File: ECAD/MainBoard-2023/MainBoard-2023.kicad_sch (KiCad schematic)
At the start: 69 parts, among them J1 XT60, J10 Conn_01x14, J11 Conn_01x03, J12 Conn_01x04, J13 Conn_01x03, J14 Conn_01x03, J15 Conn_01x03, J2 Conn_01x04, J20 BAU, J21 BAU, J22 Conn_01x04, J23 Conn_01x02, J24 Conn_01x07, J26 BAU, J27 BAU, J28 Conn_01x02, J29 Conn_01x02, J3 ConStep1, J30 Conn_01x03, J32 Conn_01x02, J37 Conn_01x02, J38 Conn_01x02, J39 Conn_01x02, J4 Conn_01x02, J40 Conn_01x02, J5 ConStep1, J6 ConStep1, J7 XT30, J8 Conn_01x02, J9 XT60, K1 CB1-P-24V, U1 Teensy3.5_All_Pins, U2 R-78B3.3-2.0, U4 R-78B5.0-2.0

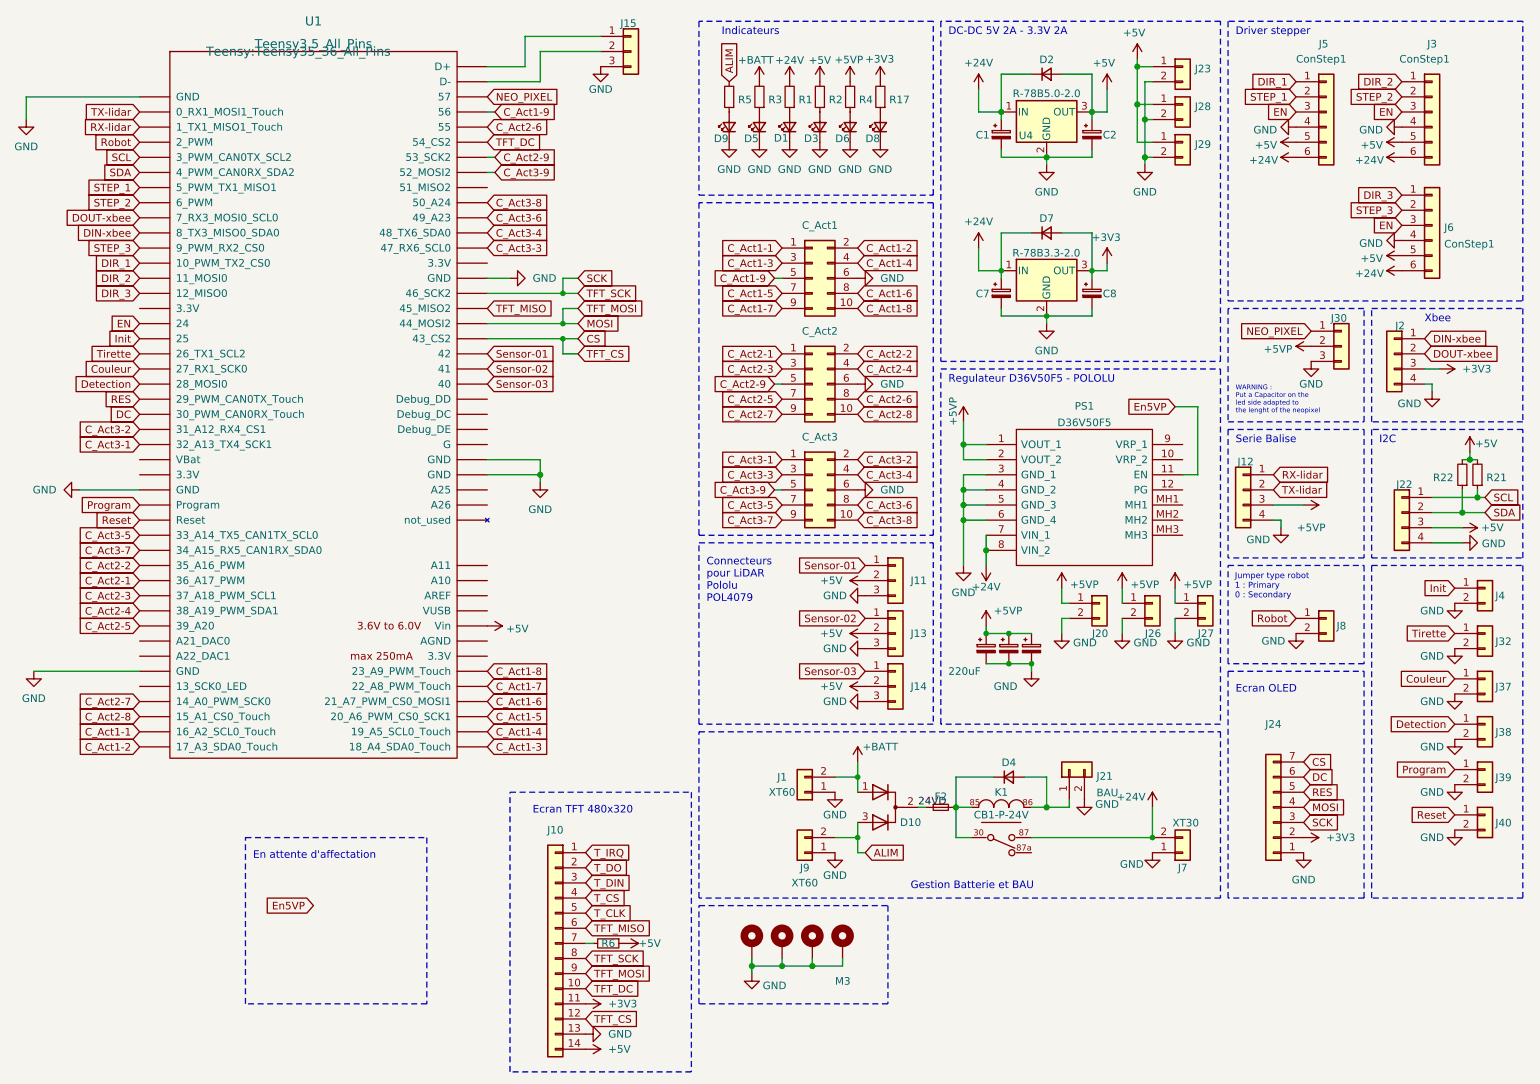
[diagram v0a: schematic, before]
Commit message: add connectors - modify pinout
add 3 power connectors XT-30 24V
modify pinout to have a minimum of 2 pwm for each sattellite connectors
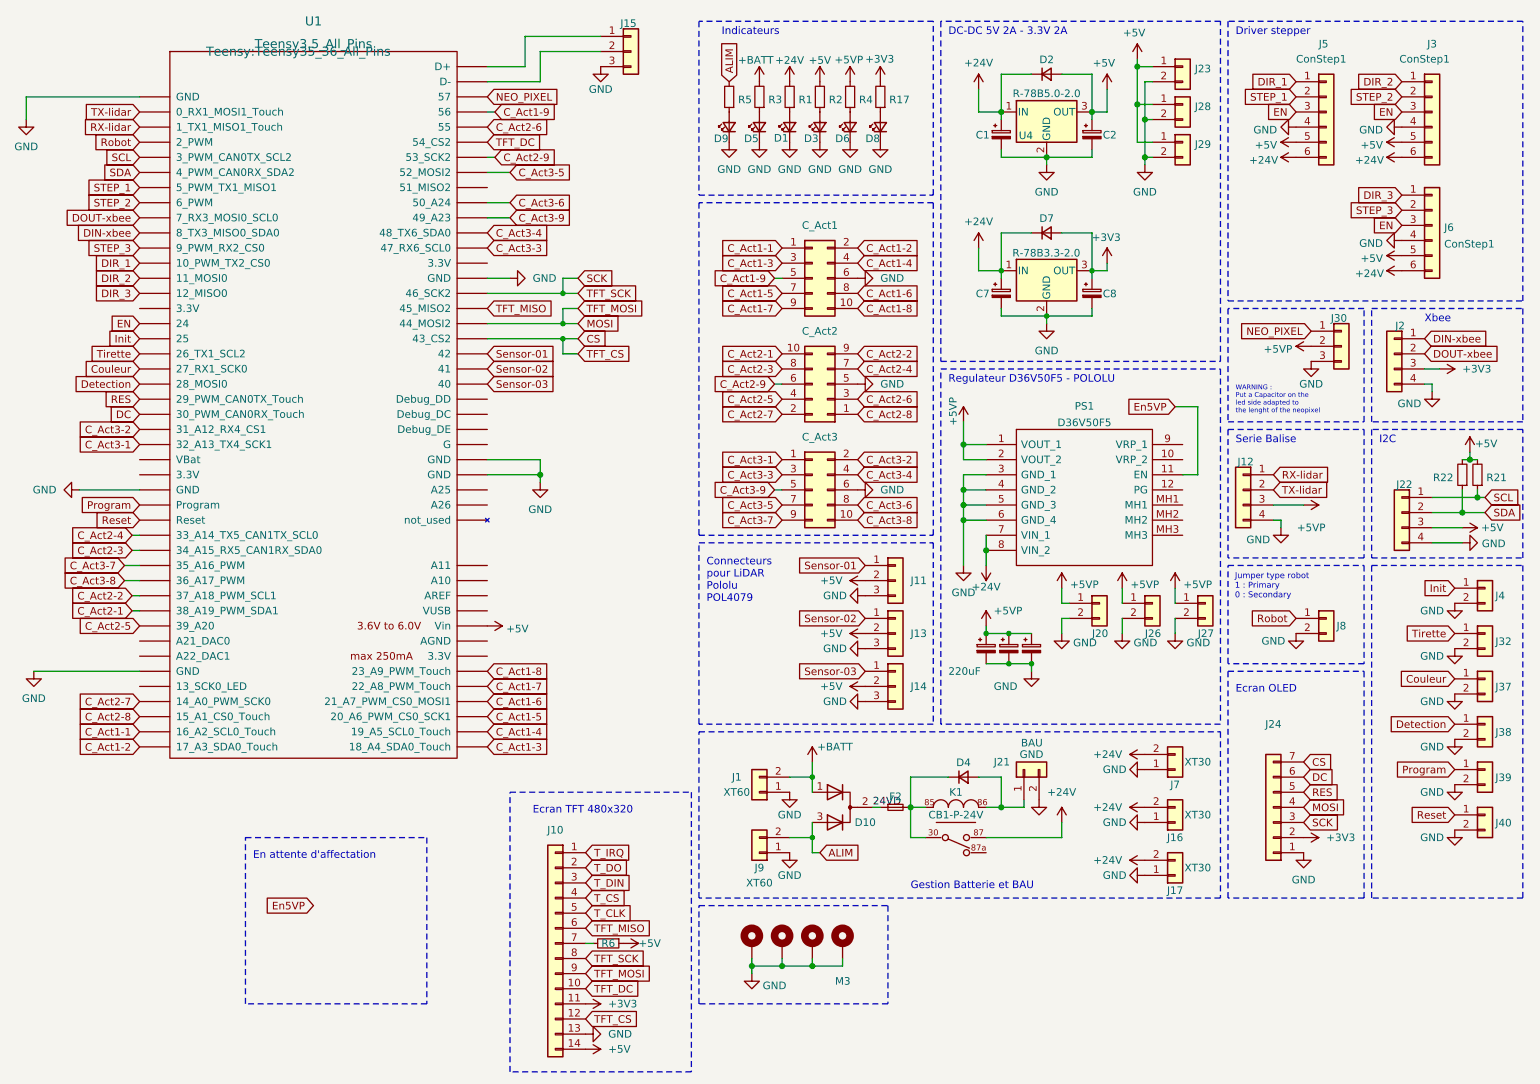
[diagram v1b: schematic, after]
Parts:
- added J16, J17: XT30, Connector_AMASS:AMASS_XT30UPB-F_1x02_P5.0mm_Vertical, symbol Connector_Generic:Conn_01x02
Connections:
- net +24V: now also J16.2 (Pin_2), J17.2 (Pin_2)
- net C_Act2-1: now also C_Act2.10 (Pin_10), U1.35 (38_A19_PWM_SDA1); no longer C_Act2.1 (Pin_1), U1.33 (36_A17_PWM)
- net C_Act2-2: now also C_Act2.9 (Pin_9), U1.34 (37_A18_PWM_SCL1); no longer C_Act2.2 (Pin_2), U1.32 (35_A16_PWM)
- net C_Act2-3: now also C_Act2.8 (Pin_8), U1.31 (34_A15_RX5_CAN1RX_SDA0); no longer C_Act2.3 (Pin_3), U1.34 (37_A18_PWM_SCL1)
- net C_Act2-4: now also C_Act2.7 (Pin_7), U1.30 (33_A14_TX5_CAN1TX_SCL0); no longer C_Act2.4 (Pin_4), U1.35 (38_A19_PWM_SDA1)
- net C_Act2-5: now also C_Act2.4 (Pin_4); no longer C_Act2.7 (Pin_7)
- net C_Act2-6: now also C_Act2.3 (Pin_3); no longer C_Act2.8 (Pin_8)
- net C_Act2-7: now also C_Act2.2 (Pin_2); no longer C_Act2.9 (Pin_9)
- net C_Act2-8: now also C_Act2.1 (Pin_1); no longer C_Act2.10 (Pin_10)
- net C_Act2-9: now also C_Act2.6 (Pin_6); no longer C_Act2.5 (Pin_5)
- net C_Act3-5: now also U1.81 (52_MOSI2); no longer U1.30 (33_A14_TX5_CAN1TX_SCL0)
- net C_Act3-6: now also U1.79 (50_A24); no longer U1.78 (49_A23)
- net C_Act3-7: now also U1.32 (35_A16_PWM); no longer U1.31 (34_A15_RX5_CAN1RX_SDA0)
- net C_Act3-8: now also U1.33 (36_A17_PWM); no longer U1.79 (50_A24)
- net C_Act3-9: now also U1.78 (49_A23); no longer U1.81 (52_MOSI2)
- net GND: now also C_Act2.5 (Pin_5), J16.1 (Pin_1), J17.1 (Pin_1); no longer C_Act2.6 (Pin_6)
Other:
- moved on the sheet: C_Act2, D10, D4, F2, J1, J21, J9, K1

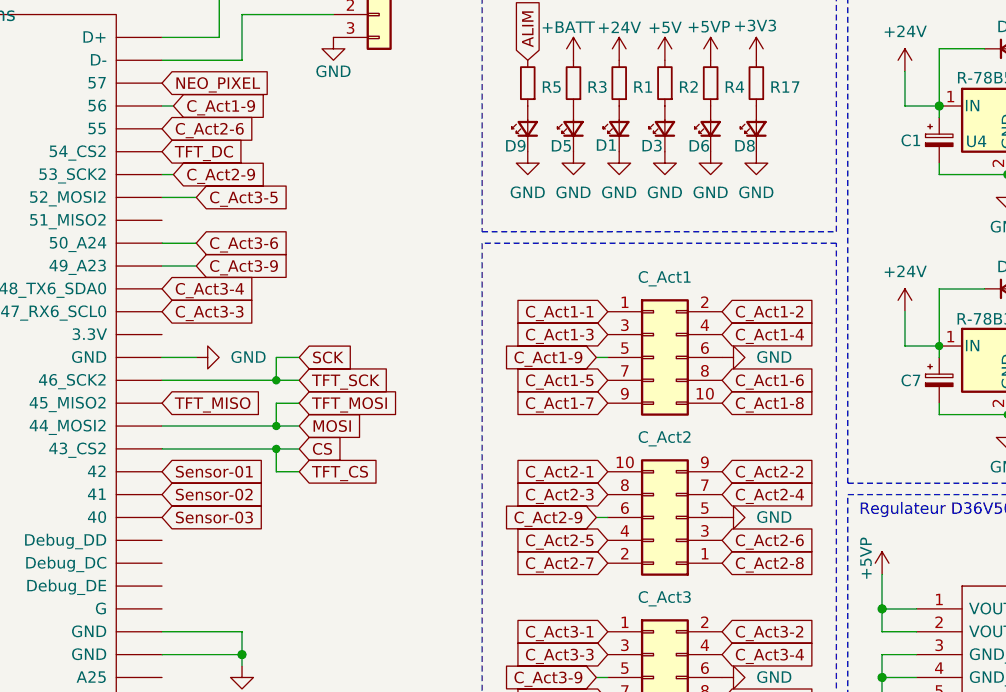
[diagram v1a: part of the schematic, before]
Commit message: Change Pinout
Change pinout for the Satellite connectors
- 2 PWM
- 4 analog
- 3 other (mix digital/analog/pwm depending on the connector)
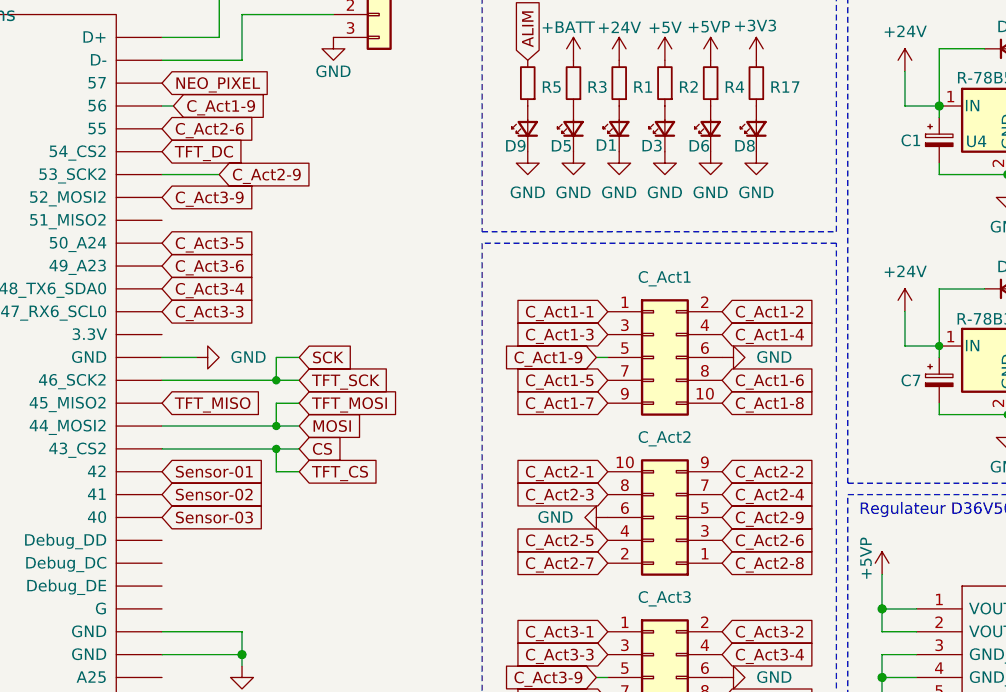
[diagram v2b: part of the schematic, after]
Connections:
- net C_Act2-9: now also C_Act2.5 (Pin_5); no longer C_Act2.6 (Pin_6)
- net C_Act3-5: now also U1.79 (50_A24); no longer U1.81 (52_MOSI2)
- net C_Act3-6: now also U1.78 (49_A23); no longer U1.79 (50_A24)
- net C_Act3-9: now also U1.81 (52_MOSI2); no longer U1.78 (49_A23)
- net GND: now also C_Act2.6 (Pin_6); no longer C_Act2.5 (Pin_5)
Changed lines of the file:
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@@
     (stroke (width 0) (type default) (color 0 0 0 0))
   )
-  (wire (pts (xy 109.22 40.64) (xy 107.95 40.64))
+  (wire (pts (xy 114.3 40.64) (xy 107.95 40.64))
     (stroke (width 0) (type default) (color 0 0 0 0))
   )
@@
     (stroke (width 0) (type dash) (color 0 0 0 0))
   )
-  (wire (pts (xy 111.76 43.18) (xy 107.95 43.18))
-    (stroke (width 0) (type default) (color 0 0 0 0))
-  )
   (polyline (pts (xy 232.41 165.1) (xy 232.41 127))
     (stroke (width 0) (type dash) (color 0 0 0 0))
@@
     (stroke (width 0) (type dash) (color 0 0 0 0))
   )
-  (wire (pts (xy 111.76 50.8) (xy 107.95 50.8))
-    (stroke (width 0) (type default) (color 0 0 0 0))
-  )
   (polyline (pts (xy 182.88 48.26) (xy 143.51 48.26))
     (stroke (width 0) (type dash) (color 0 0 0 0))
@@
     (stroke (width 0) (type default) (color 0 0 0 0))
   )
-  (wire (pts (xy 111.76 48.26) (xy 107.95 48.26))
-    (stroke (width 0) (type default) (color 0 0 0 0))
-  )
   (wire (pts (xy 48.26 114.3) (xy 49.53 114.3))
     (stroke (width 0) (type default) (color 0 0 0 0))
@@
     (stroke (width 0) (type solid) (color 0 0 0 0))
   )
-  (wire (pts (xy 156.21 78.74) (xy 157.48 78.74))
-    (stroke (width 0) (type default) (color 0 0 0 0))
-  )
   (wire (pts (xy 218.44 27.94) (xy 218.44 34.29))
     (stroke (width 0) (type solid) (color 0 0 0 0))
@@
     )
   )
-  (global_label "C_Act2-9" (shape input) (at 156.21 78.74 180) (fields_autoplaced)
-    (effects (font (size 1.27 1.27)) (justify right))
-    (property "Intersheet References" "${INTERSHEET_REFS}" (id 0) (at 144.4745 78.6606 0)
-      (effects (font (size 1.27 1.27)) (justify right) hide)
+  (global_label "C_Act2-9" (shape input) (at 170.18 78.74 0) (fields_autoplaced)
+    (effects (font (size 1.27 1.27)) (justify left))
+    (property "Intersheet References" "${INTERSHEET_REFS}" (id 0) (at 181.9155 78.8194 0)
+      (effects (font (size 1.27 1.27)) (justify left) hide)
     )
   )
@@
     )
   )
-  (global_label "C_Act3-9" (shape input) (at 111.76 50.8 0) (fields_autoplaced)
+  (global_label "C_Act3-9" (shape input) (at 107.95 43.18 0) (fields_autoplaced)
     (effects (font (size 1.27 1.27)) (justify left))
-    (property "Intersheet References" "${INTERSHEET_REFS}" (id 0) (at 123.4955 50.8794 0)
+    (property "Intersheet References" "${INTERSHEET_REFS}" (id 0) (at 119.6855 43.2594 0)
       (effects (font (size 1.27 1.27)) (justify left) hide)
     )
@@
     )
   )
-  (global_label "C_Act3-6" (shape input) (at 111.76 48.26 0) (fields_autoplaced)
+  (global_label "C_Act3-6" (shape input) (at 107.95 50.8 0) (fields_autoplaced)
     (effects (font (size 1.27 1.27)) (justify left))
-    (property "Intersheet References" "${INTERSHEET_REFS}" (id 0) (at 123.4955 48.1806 0)
+    (property "Intersheet References" "${INTERSHEET_REFS}" (id 0) (at 119.6855 50.7206 0)
       (effects (font (size 1.27 1.27)) (justify left) hide)
     )
@@
     )
   )
-  (global_label "C_Act3-5" (shape input) (at 111.76 43.18 0) (fields_autoplaced)
+  (global_label "C_Act3-5" (shape input) (at 107.95 48.26 0) (fields_autoplaced)
     (effects (font (size 1.27 1.27)) (justify left))
-    (property "Intersheet References" "${INTERSHEET_REFS}" (id 0) (at 123.4955 43.2594 0)
+    (property "Intersheet References" "${INTERSHEET_REFS}" (id 0) (at 119.6855 48.3394 0)
       (effects (font (size 1.27 1.27)) (justify left) hide)
     )
@@
     )
   )
-  (global_label "C_Act2-9" (shape input) (at 109.22 40.64 0) (fields_autoplaced)
+  (global_label "C_Act2-9" (shape input) (at 114.3 40.64 0) (fields_autoplaced)
     (effects (font (size 1.27 1.27)) (justify left))
-    (property "Intersheet References" "${INTERSHEET_REFS}" (id 0) (at 120.9555 40.7194 0)
+    (property "Intersheet References" "${INTERSHEET_REFS}" (id 0) (at 126.0355 40.7194 0)
       (effects (font (size 1.27 1.27)) (justify left) hide)
     )
@@
     (pin "1")
   )
-  (symbol (lib_id "power:GND") (at 170.18 78.74 90) (unit 1)
+  (symbol (lib_id "power:GND") (at 157.48 78.74 270) (unit 1)
     (in_bom yes) (on_board yes) (fields_autoplaced)
-    (property "Reference" "#PWR0150" (id 0) (at 176.53 78.74 0)
+    (property "Reference" "#PWR0150" (id 0) (at 151.13 78.74 0)
       (effects (font (size 1.27 1.27)) hide)
     )
-    (property "Value" "GND" (id 1) (at 173.99 78.7401 90)
+    (property "Value" "GND" (id 1) (at 153.67 78.7399 90)
       (effects (font (size 1.27 1.27)) (justify right))
     )
-    (property "Footprint" "" (id 2) (at 170.18 78.74 0)
+    (property "Footprint" "" (id 2) (at 157.48 78.74 0)
       (effects (font (size 1.27 1.27)) hide)
     )
-    (property "Datasheet" "" (id 3) (at 170.18 78.74 0)
+    (property "Datasheet" "" (id 3) (at 157.48 78.74 0)
       (effects (font (size 1.27 1.27)) hide)
     )
